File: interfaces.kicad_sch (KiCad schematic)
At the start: 84 parts, among them IC1 TPD8S009DSMR, J1 WE_629105150521, J2 685119134923, J3 1140084168, Q1 BSS138APW, Q2 BSS138APW, Q3 BSS138APW, Q4 BSS138APW, Q5 BSS138APW, U4 FT4232H-56Q, Y1 ABM8G-12.000MHZ-18-D2Y-T

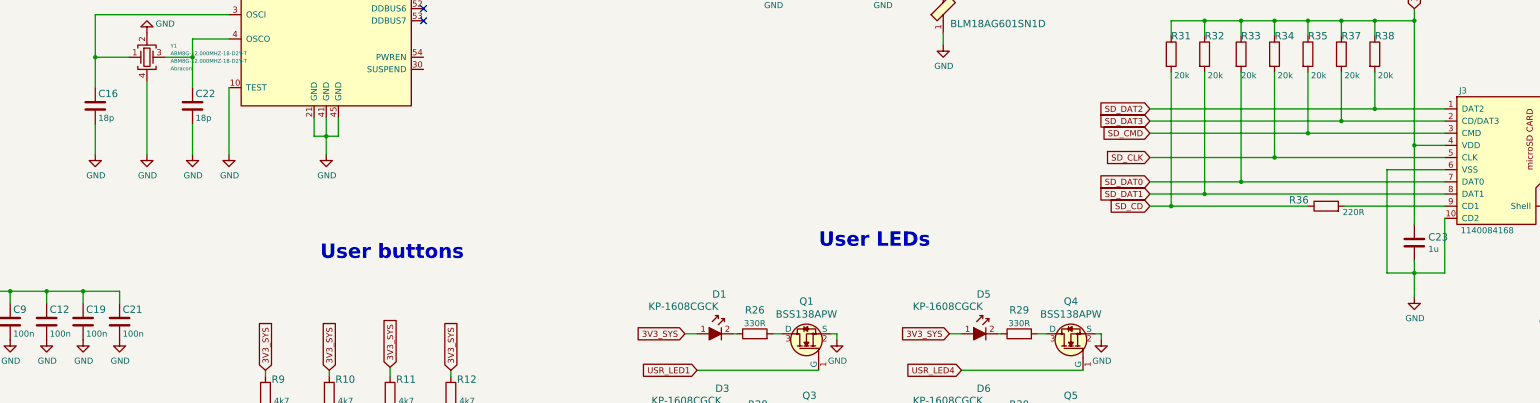
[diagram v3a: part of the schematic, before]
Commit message: Add 3d model of DDR5 testbed. Fix annotation
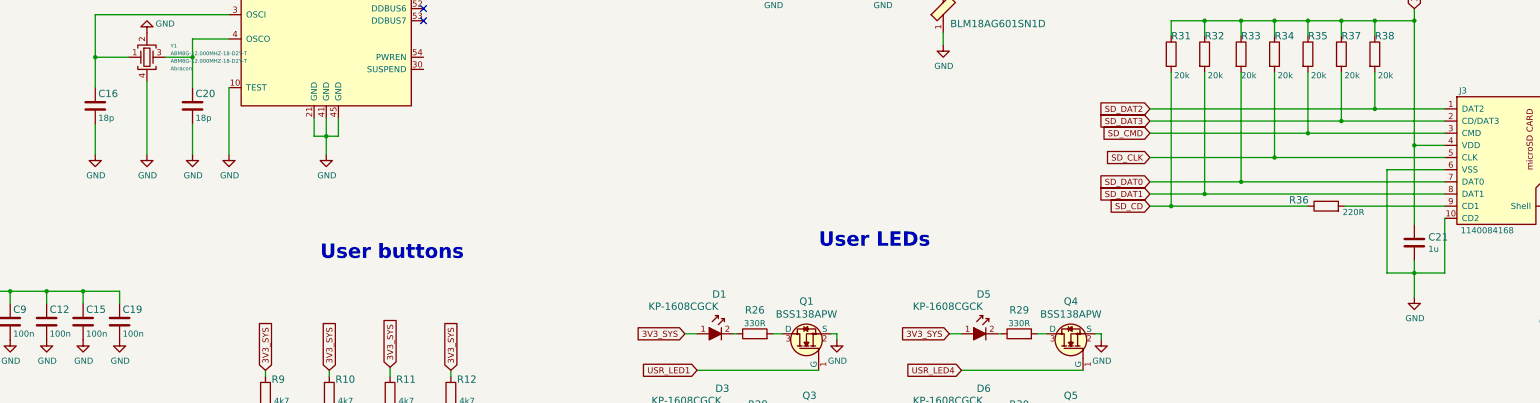
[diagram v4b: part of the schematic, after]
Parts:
- renumbered C19 to C15, C21 to C19, C22 to C20, C23 to C21
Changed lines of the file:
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@@
   (symbol (lib_id "lpddr4-test-board:GND") (at 136.525 265.43 0) (unit 1)
     (in_bom yes) (on_board yes)
-    (property "Reference" "#PWR032" (id 0) (at 136.525 271.78 0)
+    (property "Reference" "#PWR030" (id 0) (at 136.525 271.78 0)
       (effects (font (size 1.27 1.27)) hide)
     )
@@
   (symbol (lib_id "lpddr4-test-board:GND") (at 111.125 265.43 0) (unit 1)
     (in_bom yes) (on_board yes)
-    (property "Reference" "#PWR030" (id 0) (at 111.125 271.78 0)
+    (property "Reference" "#PWR028" (id 0) (at 111.125 271.78 0)
       (effects (font (size 1.27 1.27)) hide)
     )
@@
   (symbol (lib_id "lpddr4-test-board:GND") (at 97.79 265.43 0) (unit 1)
     (in_bom yes) (on_board yes)
-    (property "Reference" "#PWR028" (id 0) (at 97.79 271.78 0)
+    (property "Reference" "#PWR026" (id 0) (at 97.79 271.78 0)
       (effects (font (size 1.27 1.27)) hide)
     )
@@
   (symbol (lib_id "lpddr4-test-board:GND") (at 123.825 264.795 0) (unit 1)
     (in_bom yes) (on_board yes)
-    (property "Reference" "#PWR031" (id 0) (at 123.825 271.145 0)
+    (property "Reference" "#PWR029" (id 0) (at 123.825 271.145 0)
       (effects (font (size 1.27 1.27)) hide)
     )
@@
   (symbol (lib_id "lpddr4-test-board:GND") (at 217.17 225.425 0) (unit 1)
     (in_bom yes) (on_board yes)
-    (property "Reference" "#PWR034" (id 0) (at 217.17 231.775 0)
+    (property "Reference" "#PWR032" (id 0) (at 217.17 231.775 0)
       (effects (font (size 1.27 1.27)) hide)
     )
@@
   (symbol (lib_id "lpddr4-test-board:GND") (at 73.025 129.54 0) (unit 1)
     (in_bom yes) (on_board yes) (fields_autoplaced)
-    (property "Reference" "#PWR022" (id 0) (at 73.025 135.89 0)
+    (property "Reference" "#PWR021" (id 0) (at 73.025 135.89 0)
       (effects (font (size 1.27 1.27)) hide)
     )
@@
   (symbol (lib_id "lpddr4-test-board:C_18p_0402") (at 82.55 176.53 0) (unit 1)
     (in_bom yes) (on_board yes)
-    (property "Reference" "C22" (id 0) (at 83.185 173.99 0)
+    (property "Reference" "C20" (id 0) (at 83.185 173.99 0)
       (effects (font (size 1.524 1.524)) (justify left))
     )
@@
   (symbol (lib_id "lpddr4-test-board:GND") (at 110.49 186.69 0) (unit 1)
     (in_bom yes) (on_board yes)
-    (property "Reference" "#PWR029" (id 0) (at 110.49 193.04 0)
+    (property "Reference" "#PWR027" (id 0) (at 110.49 193.04 0)
       (effects (font (size 1.27 1.27)) hide)
     )
@@
   (symbol (lib_id "lpddr4-test-board:GND") (at 90.17 186.69 0) (unit 1)
     (in_bom yes) (on_board yes)
-    (property "Reference" "#PWR027" (id 0) (at 90.17 193.04 0)
+    (property "Reference" "#PWR025" (id 0) (at 90.17 193.04 0)
       (effects (font (size 1.27 1.27)) hide)
     )
@@
   (symbol (lib_id "lpddr4-test-board:GND") (at 82.55 186.69 0) (unit 1)
     (in_bom yes) (on_board yes)
-    (property "Reference" "#PWR026" (id 0) (at 82.55 193.04 0)
+    (property "Reference" "#PWR024" (id 0) (at 82.55 193.04 0)
       (effects (font (size 1.27 1.27)) hide)
     )
@@
   (symbol (lib_id "lpddr4-test-board:C_100n_0402_6V3") (at 59.69 221.615 0) (unit 1)
     (in_bom yes) (on_board yes)
-    (property "Reference" "C19" (id 0) (at 60.325 219.075 0)
+    (property "Reference" "C15" (id 0) (at 60.325 219.075 0)
       (effects (font (size 1.524 1.524)) (justify left))
     )
@@
   (symbol (lib_id "lpddr4-test-board:C_100n_0402_6V3") (at 67.31 221.615 0) (unit 1)
     (in_bom yes) (on_board yes)
-    (property "Reference" "C21" (id 0) (at 67.945 219.075 0)
+    (property "Reference" "C19" (id 0) (at 67.945 219.075 0)
       (effects (font (size 1.524 1.524)) (justify left))
     )
@@
   (symbol (lib_id "lpddr4-test-board:GND") (at 59.69 225.425 0) (unit 1)
     (in_bom yes) (on_board yes)
-    (property "Reference" "#PWR020" (id 0) (at 59.69 231.775 0)
+    (property "Reference" "#PWR017" (id 0) (at 59.69 231.775 0)
       (effects (font (size 1.27 1.27)) hide)
     )
@@
   (symbol (lib_id "lpddr4-test-board:GND") (at 67.31 225.425 0) (unit 1)
     (in_bom yes) (on_board yes)
-    (property "Reference" "#PWR025" (id 0) (at 67.31 231.775 0)
+    (property "Reference" "#PWR020" (id 0) (at 67.31 231.775 0)
       (effects (font (size 1.27 1.27)) hide)
     )
@@
   (symbol (lib_id "lpddr4-test-board:GND") (at 226.695 151.13 0) (unit 1)
     (in_bom yes) (on_board yes)
-    (property "Reference" "#PWR037" (id 0) (at 226.695 157.48 0)
+    (property "Reference" "#PWR035" (id 0) (at 226.695 157.48 0)
       (effects (font (size 1.27 1.27)) hide)
     )
@@
   (symbol (lib_id "lpddr4-test-board:GND") (at 239.395 163.83 0) (unit 1)
     (in_bom yes) (on_board yes)
-    (property "Reference" "#PWR038" (id 0) (at 239.395 170.18 0)
+    (property "Reference" "#PWR036" (id 0) (at 239.395 170.18 0)
       (effects (font (size 1.27 1.27)) hide)
     )
@@
   (symbol (lib_id "lpddr4-test-board:GND") (at 203.835 151.13 0) (unit 1)
     (in_bom yes) (on_board yes)
-    (property "Reference" "#PWR033" (id 0) (at 203.835 157.48 0)
+    (property "Reference" "#PWR031" (id 0) (at 203.835 157.48 0)
       (effects (font (size 1.27 1.27)) hide)
     )
@@
   (symbol (lib_id "lpddr4-test-board:GND") (at 254.635 102.235 0) (unit 1)
     (in_bom yes) (on_board yes)
-    (property "Reference" "#PWR039" (id 0) (at 254.635 108.585 0)
+    (property "Reference" "#PWR037" (id 0) (at 254.635 108.585 0)
       (effects (font (size 1.27 1.27)) hide)
     )
@@
   (symbol (lib_id "lpddr4-test-board:GND") (at 260.35 102.235 0) (unit 1)
     (in_bom yes) (on_board yes)
-    (property "Reference" "#PWR040" (id 0) (at 260.35 108.585 0)
+    (property "Reference" "#PWR038" (id 0) (at 260.35 108.585 0)
       (effects (font (size 1.27 1.27)) hide)
     )
@@
   (symbol (lib_id "lpddr4-test-board:GND") (at 280.67 102.235 0) (unit 1)
     (in_bom yes) (on_board yes)
-    (property "Reference" "#PWR043" (id 0) (at 280.67 108.585 0)
+    (property "Reference" "#PWR041" (id 0) (at 280.67 108.585 0)
       (effects (font (size 1.27 1.27)) hide)
     )
@@
   (symbol (lib_id "lpddr4-test-board:GND") (at 339.725 107.315 0) (unit 1)
     (in_bom yes) (on_board yes)
-    (property "Reference" "#PWR045" (id 0) (at 339.725 113.665 0)
+    (property "Reference" "#PWR043" (id 0) (at 339.725 113.665 0)
       (effects (font (size 1.27 1.27)) hide)
     )
@@
   (symbol (lib_id "lpddr4-test-board:GND") (at 337.82 216.535 0) (unit 1)
     (in_bom yes) (on_board yes)
-    (property "Reference" "#PWR044" (id 0) (at 337.82 222.885 0)
+    (property "Reference" "#PWR042" (id 0) (at 337.82 222.885 0)
       (effects (font (size 1.27 1.27)) hide)
     )
@@
   (symbol (lib_id "lpddr4-test-board:GND") (at 365.76 217.17 0) (unit 1)
     (in_bom yes) (on_board yes)
-    (property "Reference" "#PWR046" (id 0) (at 365.76 223.52 0)
+    (property "Reference" "#PWR044" (id 0) (at 365.76 223.52 0)
       (effects (font (size 1.27 1.27)) hide)
     )
@@
   (symbol (lib_id "lpddr4-test-board:C_1u_0603") (at 337.82 205.105 0) (unit 1)
     (in_bom yes) (on_board yes)
-    (property "Reference" "C23" (id 0) (at 340.741 203.962 0)
+    (property "Reference" "C21" (id 0) (at 340.741 203.962 0)
       (effects (font (size 1.524 1.524)) (justify left))
     )
@@
   (symbol (lib_id "lpddr4-test-board:GND") (at 73.025 186.69 0) (unit 1)
     (in_bom yes) (on_board yes)
-    (property "Reference" "#PWR024" (id 0) (at 73.025 193.04 0)
+    (property "Reference" "#PWR023" (id 0) (at 73.025 193.04 0)
       (effects (font (size 1.27 1.27)) hide)
     )
@@
   (symbol (lib_id "lpddr4-test-board:GND") (at 73.025 161.29 180) (unit 1)
     (in_bom yes) (on_board yes)
-    (property "Reference" "#PWR023" (id 0) (at 73.025 154.94 0)
+    (property "Reference" "#PWR022" (id 0) (at 73.025 154.94 0)
       (effects (font (size 1.27 1.27)) hide)
     )
@@
   (symbol (lib_id "lpddr4-test-board:GND") (at 217.17 264.795 0) (unit 1)
     (in_bom yes) (on_board yes)
-    (property "Reference" "#PWR035" (id 0) (at 217.17 271.145 0)
+    (property "Reference" "#PWR033" (id 0) (at 217.17 271.145 0)
       (effects (font (size 1.27 1.27)) hide)
     )
@@
   (symbol (lib_id "lpddr4-test-board:GND") (at 272.415 245.11 0) (unit 1)
     (in_bom yes) (on_board yes)
-    (property "Reference" "#PWR042" (id 0) (at 272.415 251.46 0)
+    (property "Reference" "#PWR040" (id 0) (at 272.415 251.46 0)
       (effects (font (size 1.27 1.27)) hide)
     )
@@
   (symbol (lib_id "lpddr4-test-board:GND") (at 272.415 225.425 0) (unit 1)
     (in_bom yes) (on_board yes)
-    (property "Reference" "#PWR041" (id 0) (at 272.415 231.775 0)
+    (property "Reference" "#PWR039" (id 0) (at 272.415 231.775 0)
       (effects (font (size 1.27 1.27)) hide)
     )
@@
   (symbol (lib_id "lpddr4-test-board:GND") (at 217.805 245.11 0) (unit 1)
     (in_bom yes) (on_board yes)
-    (property "Reference" "#PWR036" (id 0) (at 217.805 251.46 0)
-      (effects (font (size 1.27 1.27)) hide)
-    )
+    (property "Reference" "#PWR034" (id 0) (at 217.805 251.46 0)
+      (effects (font (size 1.27 1.27)) hide)
+    )
